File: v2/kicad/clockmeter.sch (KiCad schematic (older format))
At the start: 14 parts, among them Y1 20M

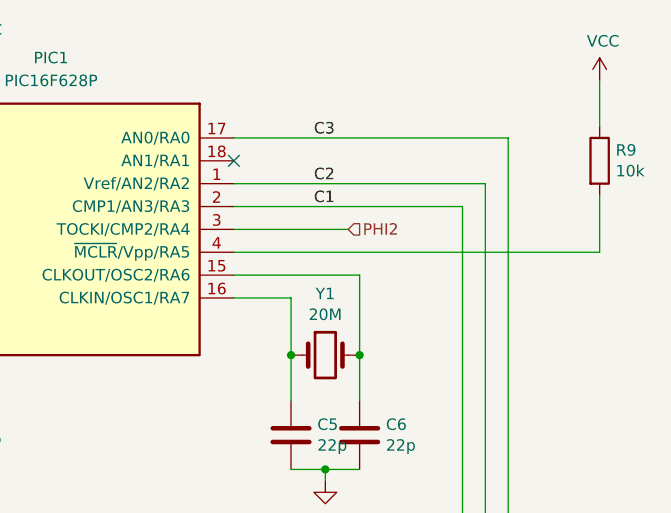
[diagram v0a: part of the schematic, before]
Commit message: Changing to Dual CIA
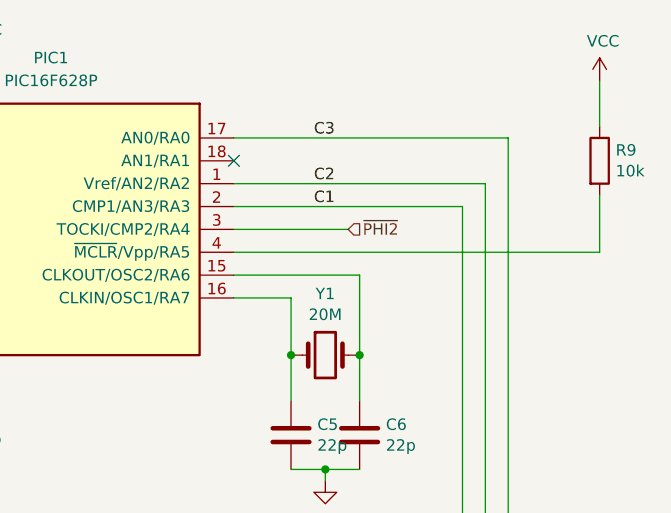
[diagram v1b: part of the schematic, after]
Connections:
- net PHI2 renamed ~PHI2
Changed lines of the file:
@@
 $Descr A4 11693 8268
 encoding utf-8
-Sheet 7 10
+Sheet 10 10
 Title ""
 Date ""
@@
 	7050 2400 7550 2400
 Text HLabel 7550 2400 2    50   Input ~ 0
-PHI2
+~PHI2
 $Comp
 L Device:R R9
